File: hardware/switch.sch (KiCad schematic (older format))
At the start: 7 parts, among them Q7 BSS138

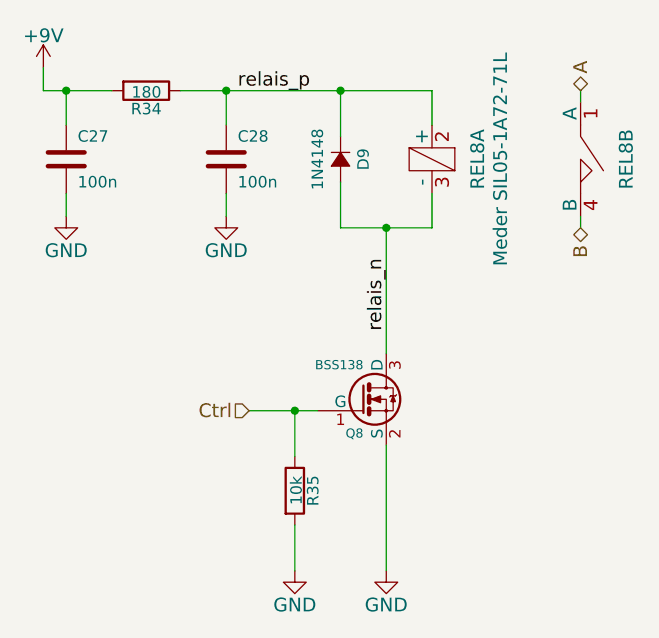
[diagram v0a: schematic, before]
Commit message: Fix major footprint fuckups...
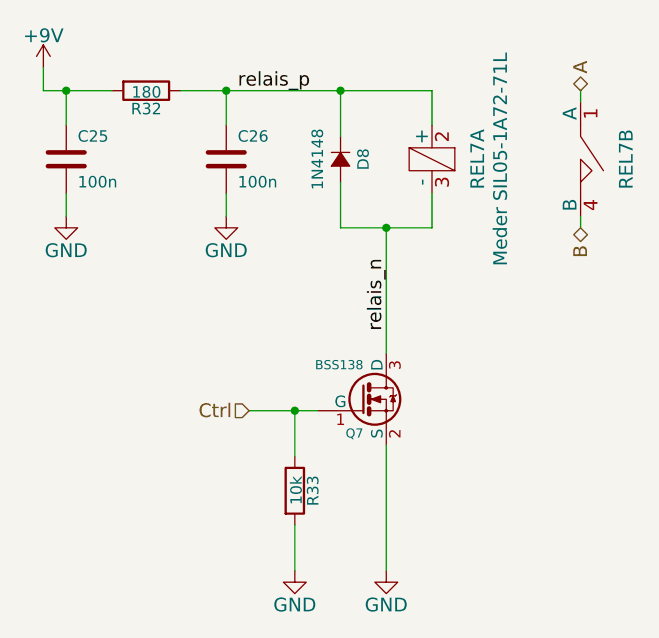
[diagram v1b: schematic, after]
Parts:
- REL7: footprint Socket_Strips:Socket_Strip_Straight_1x04 -> uMIDI-switcher:Meder_SIL
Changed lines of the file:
@@
 AR Path="/56223B06/54E8DEE8" Ref="Q7"  Part="1"
 AR Path="/56223B14/54E8DEE8" Ref="Q8"  Part="1"
-F 0 "Q8" H 5400 3201 40  0000 R CNN
+F 0 "Q7" H 5400 3201 40  0000 R CNN
 F 1 "BSS138" H 5400 3500 40  0000 R CNN
 F 2 "Housings_SOT-23_SOT-143_TSOT-6:SOT-23" H 5270 3452 29  0001 C CNN
@@
 AR Path="/56223B06/54E8DF2C" Ref="R33"  Part="1"
 AR Path="/56223B14/54E8DF2C" Ref="R35"  Part="1"
-F 0 "R35" V 5180 3750 50  0000 C CNN
+F 0 "R33" V 5180 3750 50  0000 C CNN
 F 1 "10k" V 5107 3751 50  0000 C CNN
 F 2 "Resistors_SMD:R_0603" V 5030 3750 30  0001 C CNN
@@
 $EndComp
 $Comp
-L GND #PWR81
+L GND #PWR078
 U 1 1 54E8DF95
 P 5100 4100
-AR Path="/56223B06/54E8DF95" Ref="#PWR81"  Part="1"
-AR Path="/56223B14/54E8DF95" Ref="#PWR86"  Part="1"
-F 0 "#PWR86" H 5100 3850 60  0001 C CNN
+AR Path="/56223B06/54E8DF95" Ref="#PWR078"  Part="1"
+AR Path="/56223B14/54E8DF95" Ref="#PWR083"  Part="1"
+F 0 "#PWR078" H 5100 3850 60  0001 C CNN
 F 1 "GND" H 5100 3950 60  0000 C CNN
 F 2 "" H 5100 4100 60  0000 C CNN
@@
 AR Path="/56223B06/54E8E18C" Ref="C25"  Part="1"
 AR Path="/56223B14/54E8E18C" Ref="C27"  Part="1"
-F 0 "C27" H 4150 2400 50  0000 L CNN
+F 0 "C25" H 4150 2400 50  0000 L CNN
 F 1 "100n" H 4150 2200 50  0000 L CNN
 F 2 "Capacitors_SMD:C_0603" H 4138 2150 30  0001 C CNN
@@
 AR Path="/56223B06/54E8E1C0" Ref="R32"  Part="1"
 AR Path="/56223B14/54E8E1C0" Ref="R34"  Part="1"
-F 0 "R34" V 4530 2000 50  0000 C CNN
+F 0 "R32" V 4530 2000 50  0000 C CNN
 F 1 "180" V 4457 2001 50  0000 C CNN
 F 2 "Resistors_SMD:R_0603" V 4380 2000 30  0001 C CNN
@@
 AR Path="/56223B06/54E8E27F" Ref="C26"  Part="1"
 AR Path="/56223B14/54E8E27F" Ref="C28"  Part="1"
-F 0 "C28" H 4850 2400 50  0000 L CNN
+F 0 "C26" H 4850 2400 50  0000 L CNN
 F 1 "100n" H 4850 2200 50  0000 L CNN
 F 2 "Capacitors_SMD:C_0603" H 4838 2150 30  0001 C CNN
@@
 $EndComp
 $Comp
-L GND #PWR79
+L GND #PWR079
 U 1 1 54E8E35E
 P 4100 2550
-AR Path="/56223B06/54E8E35E" Ref="#PWR79"  Part="1"
-AR Path="/56223B14/54E8E35E" Ref="#PWR84"  Part="1"
-F 0 "#PWR84" H 4100 2300 60  0001 C CNN
+AR Path="/56223B06/54E8E35E" Ref="#PWR079"  Part="1"
+AR Path="/56223B14/54E8E35E" Ref="#PWR084"  Part="1"
+F 0 "#PWR079" H 4100 2300 60  0001 C CNN
 F 1 "GND" H 4100 2400 60  0000 C CNN
 F 2 "" H 4100 2550 60  0000 C CNN
@@
 $EndComp
 $Comp
-L +9V #PWR78
+L +9V #PWR080
 U 1 1 54E8E5BD
 P 4000 1900
-AR Path="/56223B06/54E8E5BD" Ref="#PWR78"  Part="1"
-AR Path="/56223B14/54E8E5BD" Ref="#PWR83"  Part="1"
-F 0 "#PWR83" H 4000 1750 60  0001 C CNN
+AR Path="/56223B06/54E8E5BD" Ref="#PWR080"  Part="1"
+AR Path="/56223B14/54E8E5BD" Ref="#PWR085"  Part="1"
+F 0 "#PWR080" H 4000 1750 60  0001 C CNN
 F 1 "+9V" H 4000 2040 60  0000 C CNN
 F 2 "" H 4000 1900 60  0000 C CNN
@@
 $EndComp
 $Comp
-L GND #PWR82
+L GND #PWR081
 U 1 1 54E8E61E
 P 5500 4100
-AR Path="/56223B06/54E8E61E" Ref="#PWR82"  Part="1"
-AR Path="/56223B14/54E8E61E" Ref="#PWR87"  Part="1"
-F 0 "#PWR87" H 5500 3850 60  0001 C CNN
+AR Path="/56223B06/54E8E61E" Ref="#PWR081"  Part="1"
+AR Path="/56223B14/54E8E61E" Ref="#PWR086"  Part="1"
+F 0 "#PWR081" H 5500 3850 60  0001 C CNN
 F 1 "GND" H 5500 3950 60  0000 C CNN
 F 2 "" H 5500 4100 60  0000 C CNN
@@
 AR Path="/56223B06/54E8EB7A" Ref="D8"  Part="1"
 AR Path="/56223B14/54E8EB7A" Ref="D9"  Part="1"
-F 0 "D9" H 5300 2400 50  0000 C CNN
+F 0 "D8" H 5300 2400 50  0000 C CNN
 F 1 "1N4148" H 5300 2200 50  0000 C CNN
 F 2 "Diodes_SMD:SOD-123" H 5300 2300 60  0001 C CNN
@@
 $EndComp
 $Comp
-L GND #PWR80
+L GND #PWR082
 U 1 1 54E8ED21
 P 4800 2550
-AR Path="/56223B06/54E8ED21" Ref="#PWR80"  Part="1"
-AR Path="/56223B14/54E8ED21" Ref="#PWR85"  Part="1"
-F 0 "#PWR85" H 4800 2300 60  0001 C CNN
+AR Path="/56223B06/54E8ED21" Ref="#PWR082"  Part="1"
+AR Path="/56223B14/54E8ED21" Ref="#PWR087"  Part="1"
+F 0 "#PWR082" H 4800 2300 60  0001 C CNN
 F 1 "GND" H 4800 2400 60  0000 C CNN
 F 2 "" H 4800 2550 60  0000 C CNN
@@
 AR Path="/56223B06/54E8CCF9" Ref="REL7"  Part="1"
 AR Path="/56223B14/54E8CCF9" Ref="REL8"  Part="1"
-F 0 "REL8" H 5700 2500 60  0000 C CNN
+F 0 "REL7" H 5700 2500 60  0000 C CNN
 F 1 "Meder SIL05-1A72-71L" H 5700 2600 60  0000 C CNN
-F 2 "Socket_Strips:Socket_Strip_Straight_1x04" H 5700 2300 60  0001 C CNN
+F 2 "uMIDI-switcher:Meder_SIL" H 5700 2300 60  0001 C CNN
 F 3 "" H 5700 2300 60  0000 C CNN
 F 4 "Reichelt" H 5700 2300 60  0001 C CNN "Supplier"
@@
 AR Path="/56223B06/54E8CD35" Ref="REL7"  Part="2"
 AR Path="/56223B14/54E8CD35" Ref="REL8"  Part="2"
-F 0 "REL8" H 6350 2500 60  0000 C CNN
+F 0 "REL7" H 6350 2500 60  0000 C CNN
 F 1 "Meder SIL05-1A72-71L" H 6350 2000 60  0001 C CNN
-F 2 "Socket_Strips:Socket_Strip_Straight_1x04" H 6350 2300 60  0001 C CNN
+F 2 "uMIDI-switcher:Meder_SIL" H 6350 2300 60  0001 C CNN
 F 3 "" H 6350 2300 60  0000 C CNN
 F 4 "Reichelt" H 6350 2300 60  0001 C CNN "Supplier"
